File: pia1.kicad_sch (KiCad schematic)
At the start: 33 parts, among them IC20 MC14529B, IC24 74LS244N, IC25 LM393P, IC26 MC6821

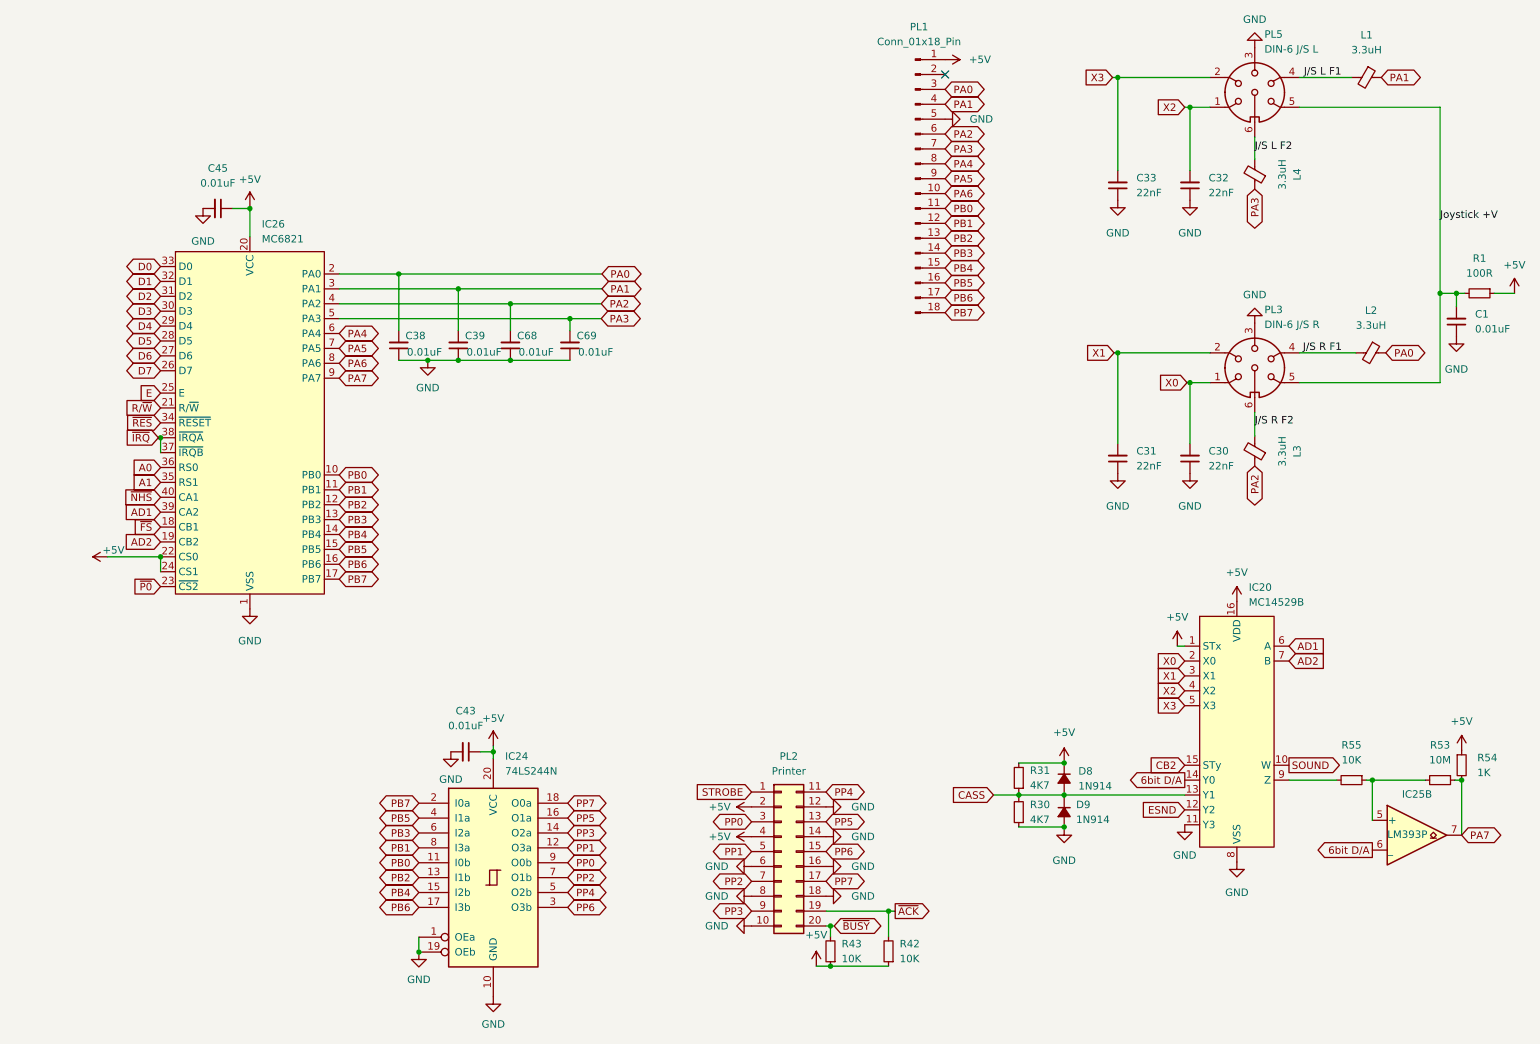
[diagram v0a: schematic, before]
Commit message: add uart to board
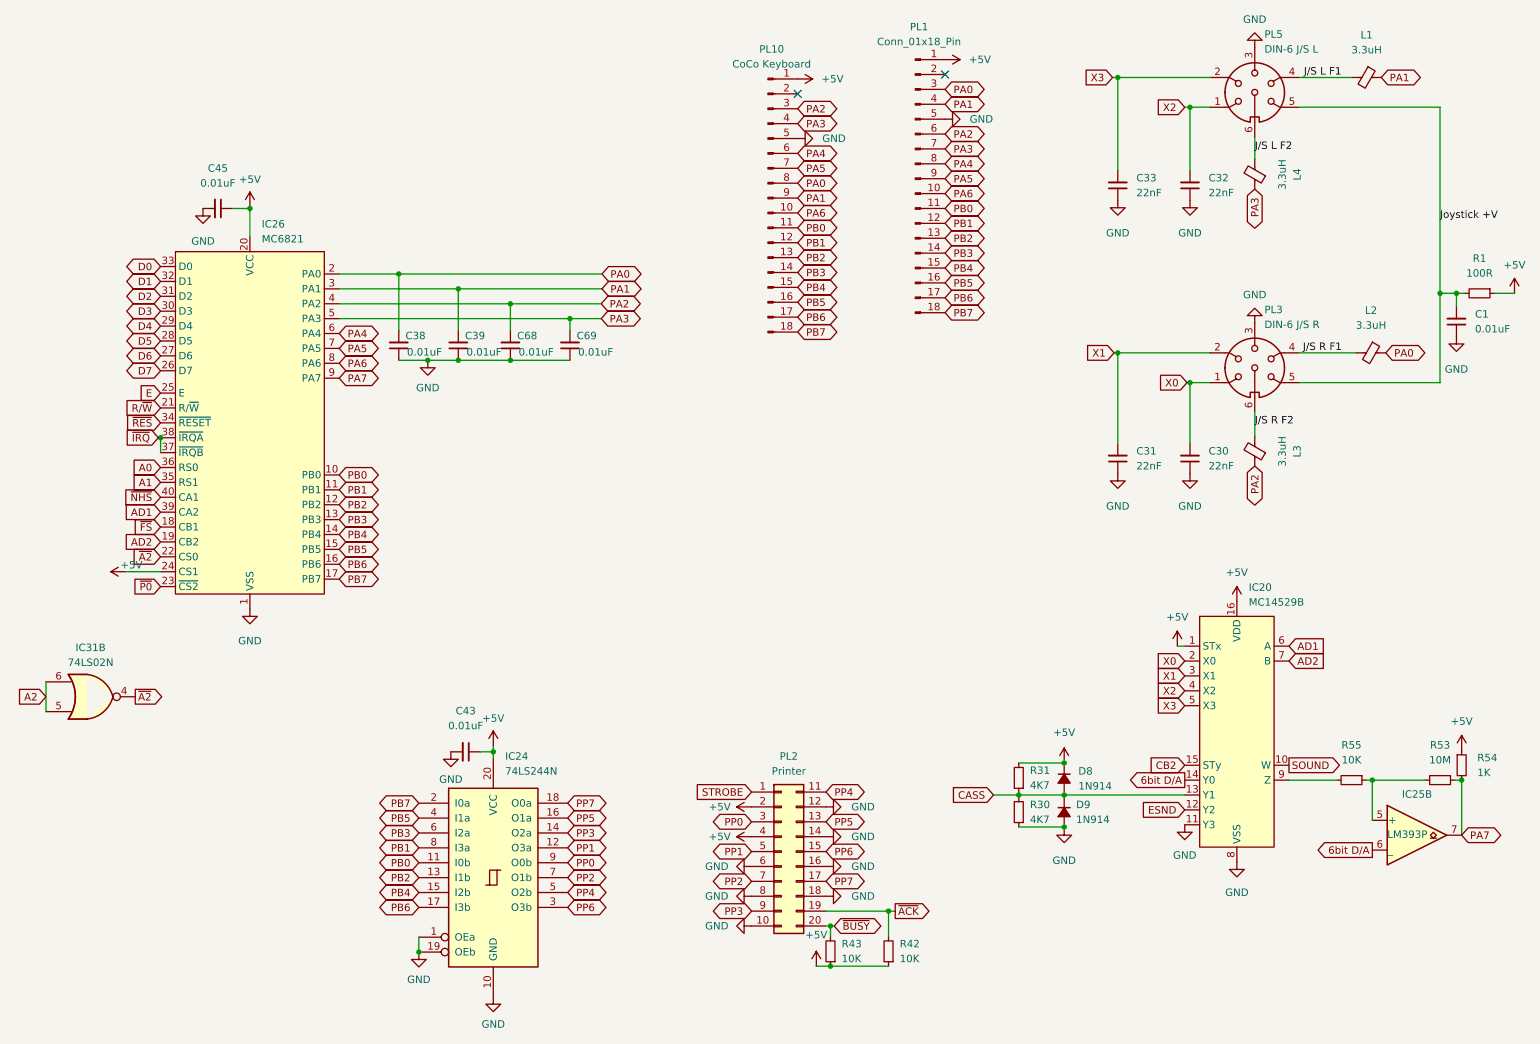
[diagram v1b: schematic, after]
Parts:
- added IC31: 74LS02N, Package_DIP:DIP-14_W7.62mm, symbol 74xx:74LS02
- added PL10: CoCo Keyboard, Connector_PinHeader_2.54mm:PinHeader_1x18_P2.54mm_Vertical, symbol Connector:Conn_01x18_Pin
- C30, C31, C32, C33: footprint Capacitor_THT:C_Disc_D5.0mm_W2.5mm_P5.00mm -> PCM_Capacitor_SMD_AKL:C_0805_2012Metric_Pad1.18x1.45mm_HandSolder; DigiKey BC2677CT-ND -> (none)
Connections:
- net +5V: now also PL10.1 (Pin_1); no longer IC26.22 (CS0)
- net GND: now also PL10.5 (Pin_5)
- net PA0: now also PL10.8 (Pin_8)
- net PA1: now also PL10.9 (Pin_9)
- net PA2: now also PL10.3 (Pin_3)
- net PA3: now also PL10.4 (Pin_4)
- net PA4: now also PL10.6 (Pin_6)
- net PA5: now also PL10.7 (Pin_7)
- net PA6: now also PL10.10 (Pin_10)
- net PB0: now also PL10.11 (Pin_11)
- net PB1: now also PL10.12 (Pin_12)
- net PB2: now also PL10.13 (Pin_13)
- net PB3: now also PL10.14 (Pin_14)
- net PB4: now also PL10.15 (Pin_15)
- net PB5: now also PL10.16 (Pin_16)
- net PB6: now also PL10.17 (Pin_17)
- net PB7: now also PL10.18 (Pin_18)
- new net A2: IC31.5, IC31.6
- new net ~{A2}: IC26.22 (CS0), IC31.4
- no-connect marks 1 -> 2

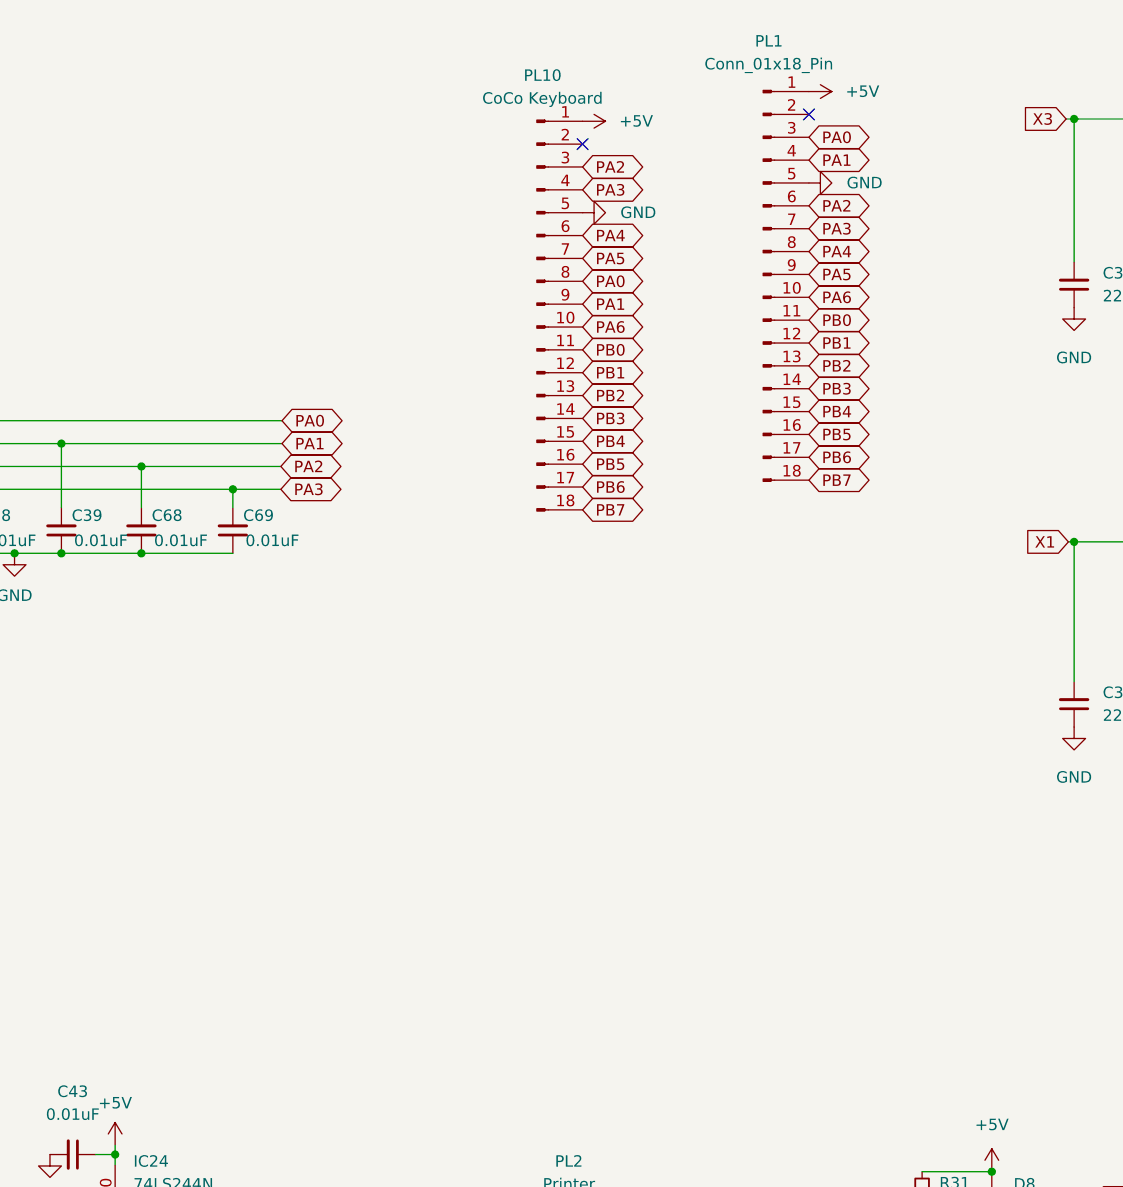
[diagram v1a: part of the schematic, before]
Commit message: rework keyboard type selection
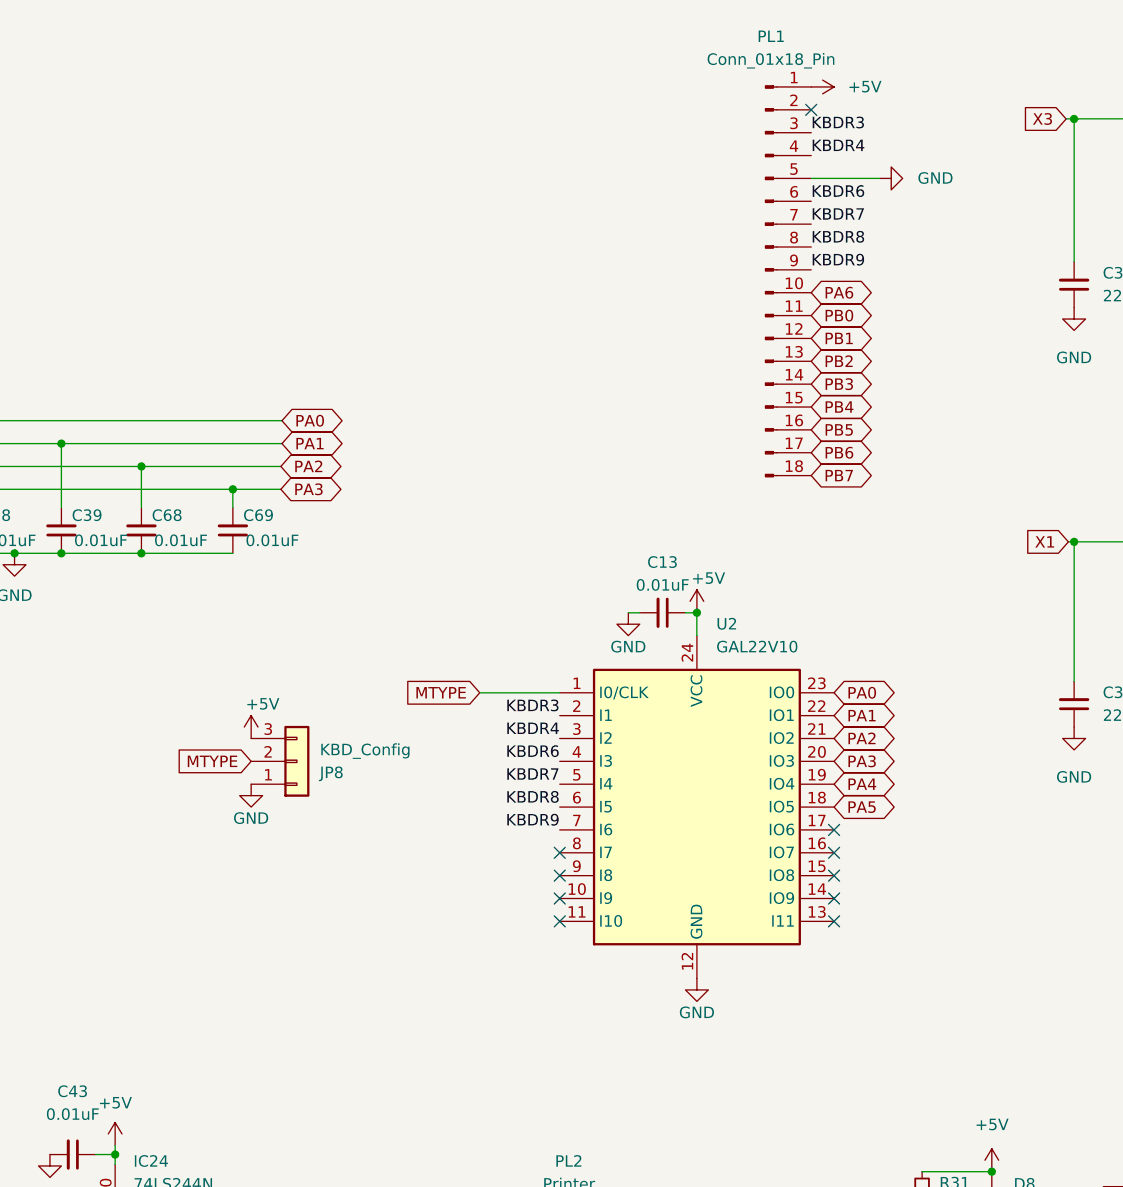
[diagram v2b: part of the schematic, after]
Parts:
- removed PL10: CoCo Keyboard, Connector_PinHeader_2.54mm:PinHeader_1x18_P2.54mm_Vertical, symbol Connector:Conn_01x18_Pin
- added C13: 0.01uF, Capacitor_THT:C_Disc_D4.3mm_W1.9mm_P5.00mm, symbol Device:C_Small
- added JP8: KBD_Config, Connector_PinHeader_2.54mm:PinHeader_1x03_P2.54mm_Vertical, symbol Connector_Generic:Conn_01x03
- added U2: GAL22V10, Package_DIP:DIP-24_W7.62mm, symbol vdg:GAL22V10
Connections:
- net +5V: now also C13.1, JP8.3 (Pin_3), U2.24 (VCC)
- net GND: now also C13.2, JP8.1 (Pin_1), U2.12 (GND)
- net PA0: now also U2.23 (IO0); no longer PL1.3 (Pin_3)
- net PA1: now also U2.22 (IO1); no longer PL1.4 (Pin_4)
- net PA2: now also U2.21 (IO2); no longer PL1.6 (Pin_6)
- net PA3: now also U2.20 (IO3); no longer PL1.7 (Pin_7)
- net PA4: now also U2.19 (IO4); no longer PL1.8 (Pin_8)
- net PA5: now also U2.18 (IO5); no longer PL1.9 (Pin_9)
- new net KBDR3: PL1.3 (Pin_3), U2.2 (I1)
- new net KBDR4: PL1.4 (Pin_4), U2.3 (I2)
- new net KBDR6: PL1.6 (Pin_6), U2.4 (I3)
- new net KBDR7: PL1.7 (Pin_7), U2.5 (I4)
- new net KBDR8: PL1.8 (Pin_8), U2.6 (I5)
- new net KBDR9: PL1.9 (Pin_9), U2.7 (I6)
- new net MTYPE: JP8.2 (Pin_2), U2.1 (I0/CLK)
- no-connect marks 2 -> 10
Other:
- moved on the sheet: PL1

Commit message: tidy up
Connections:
- net GND: now also U2.13 (I11), U2.14 (IO9), U2.15 (IO8), U2.16 (IO7), U2.17 (IO6)
- no-connect marks 10 -> 5
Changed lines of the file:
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@@
 	)
 	(junction
+		(at 181.61 111.76)
+		(diameter 0)
+		(color 0 0 0 0)
+	)
+	(junction
 		(at 265.684 145.034)
 		(diameter 0)
@@
 	)
 	(junction
+		(at 181.61 114.3)
+		(diameter 0)
+		(color 0 0 0 0)
+	)
+	(junction
 		(at 264.795 61.976)
 		(diameter 0)
@@
 	)
 	(junction
+		(at 181.61 106.68)
+		(diameter 0)
+		(color 0 0 0 0)
+	)
+	(junction
 		(at 197.866 147.574)
 		(diameter 0)
@@
 	)
 	(junction
+		(at 181.61 109.22)
+		(diameter 0)
+		(color 0 0 0 0)
+	)
+	(junction
 		(at 165.1 80.01)
 		(diameter 0)
@@
 	)
 	(no_connect
-		(at 180.34 111.76)
-	)
-	(no_connect
-		(at 180.34 109.22)
-	)
-	(no_connect
 		(at 177.8 24.13)
 	)
 	(no_connect
-		(at 180.34 114.3)
-	)
-	(no_connect
 		(at 149.86 114.3)
 	)
 	(no_connect
-		(at 180.34 106.68)
-	)
-	(no_connect
 		(at 149.86 111.76)
 	)
@@
 		(at 149.86 109.22)
 	)
-	(no_connect
-		(at 180.34 104.14)
-	)
 	(wire
 		(pts
@@
 	(wire
 		(pts
+			(xy 180.34 104.14) (xy 181.61 104.14)
+		)
+		(stroke
+			(width 0)
+			(type default)
+		)
+	)
+	(wire
+		(pts
 			(xy 74.168 61.214) (xy 94.488 61.214)
 		)
@@
 	(wire
 		(pts
+			(xy 181.61 111.76) (xy 181.61 114.3)
+		)
+		(stroke
+			(width 0)
+			(type default)
+		)
+	)
+	(wire
+		(pts
 			(xy 197.866 147.955) (xy 197.866 147.574)
 		)
@@
 	(wire
 		(pts
+			(xy 181.61 109.22) (xy 181.61 111.76)
+		)
+		(stroke
+			(width 0)
+			(type default)
+		)
+	)
+	(wire
+		(pts
 			(xy 113.538 66.294) (xy 113.538 68.326)
 		)
@@
 	(wire
 		(pts
+			(xy 180.34 106.68) (xy 181.61 106.68)
+		)
+		(stroke
+			(width 0)
+			(type default)
+		)
+	)
+	(wire
+		(pts
 			(xy 207.01 25.146) (xy 222.758 25.146)
 		)
@@
 	(wire
 		(pts
+			(xy 181.61 106.68) (xy 181.61 109.22)
+		)
+		(stroke
+			(width 0)
+			(type default)
+		)
+	)
+	(wire
+		(pts
 			(xy 274.701 61.976) (xy 271.272 61.976)
 		)
@@
 	(wire
 		(pts
+			(xy 180.34 109.22) (xy 181.61 109.22)
+		)
+		(stroke
+			(width 0)
+			(type default)
+		)
+	)
+	(wire
+		(pts
 			(xy 167.894 167.386) (xy 157.226 167.386)
 		)
@@
 	(wire
 		(pts
+			(xy 181.61 114.3) (xy 181.61 116.84)
+		)
+		(stroke
+			(width 0)
+			(type default)
+		)
+	)
+	(wire
+		(pts
 			(xy 118.872 63.754) (xy 103.378 63.754)
 		)
@@
 	(wire
 		(pts
+			(xy 180.34 114.3) (xy 181.61 114.3)
+		)
+		(stroke
+			(width 0)
+			(type default)
+		)
+	)
+	(wire
+		(pts
+			(xy 181.61 104.14) (xy 181.61 106.68)
+		)
+		(stroke
+			(width 0)
+			(type default)
+		)
+	)
+	(wire
+		(pts
 			(xy 103.378 63.754) (xy 74.168 63.754)
 		)
@@
 	(wire
 		(pts
+			(xy 180.34 111.76) (xy 181.61 111.76)
+		)
+		(stroke
+			(width 0)
+			(type default)
+		)
+	)
+	(wire
+		(pts
 			(xy 250.444 145.034) (xy 250.444 151.892)
 		)
@@
 					(unit 1)
 				)
+			)
+		)
+	)
+	(symbol
+		(lib_id "power:GND")
+		(at 181.61 116.84 0)
+		(unit 1)
+		(exclude_from_sim no)
+		(in_bom yes)
+		(on_board yes)
+		(dnp no)
+		(property "Reference" "#PWR073"
+			(at 181.61 123.19 0)
+			(effects
+				(font
+					(size 1.27 1.27)
+				)
+				(hide yes)
+			)
+		)
+		(property "Value" "GND"
+			(at 181.61 120.65 0)
+			(effects
+				(font
+					(size 1.27 1.27)
+				)
+			)
+		)
+		(property "Footprint" ""
+			(at 181.61 116.84 0)
+			(effects
+				(font
+					(size 1.27 1.27)
+				)
+				(hide yes)
+			)
+		)
+		(property "Datasheet" ""
+			(at 181.61 116.84 0)
+			(effects
+				(font
+					(size 1.27 1.27)
+				)
+				(hide yes)
+			)
+		)
+		(property "Description" ""
+			(at 181.61 116.84 0)
+			(effects
+				(font
+					(size 1.27 1.27)
+				)
+				(hide yes)
+			)
+		)
+		(pin "1"
+		)
+		(instances
+			(project "Dragon32"
+				(path "/0c3dceba-7c95-4b3d-b590-0eb581444beb/64d8d7b7-14ab-4042-9ee8-f1aec24a139c"
+					(reference "#PWR073")
+					(unit 1)
+				)

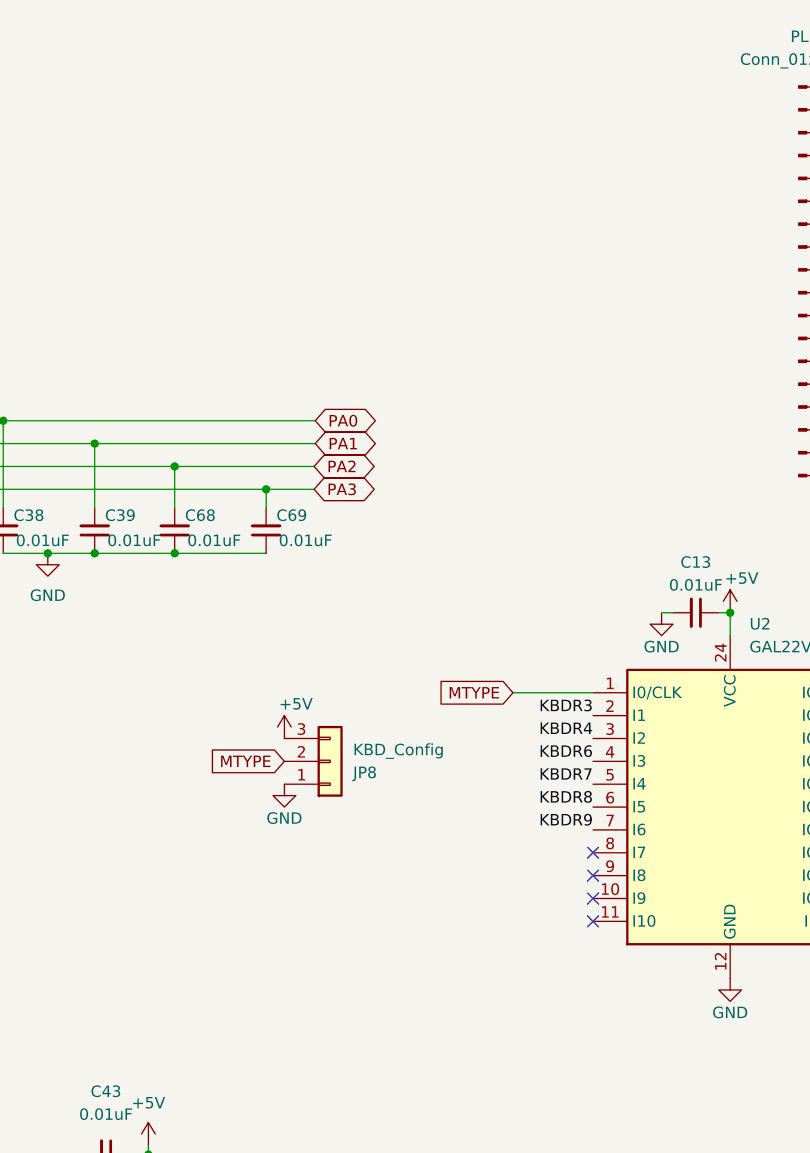
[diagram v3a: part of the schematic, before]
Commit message: pull up keyboard connections
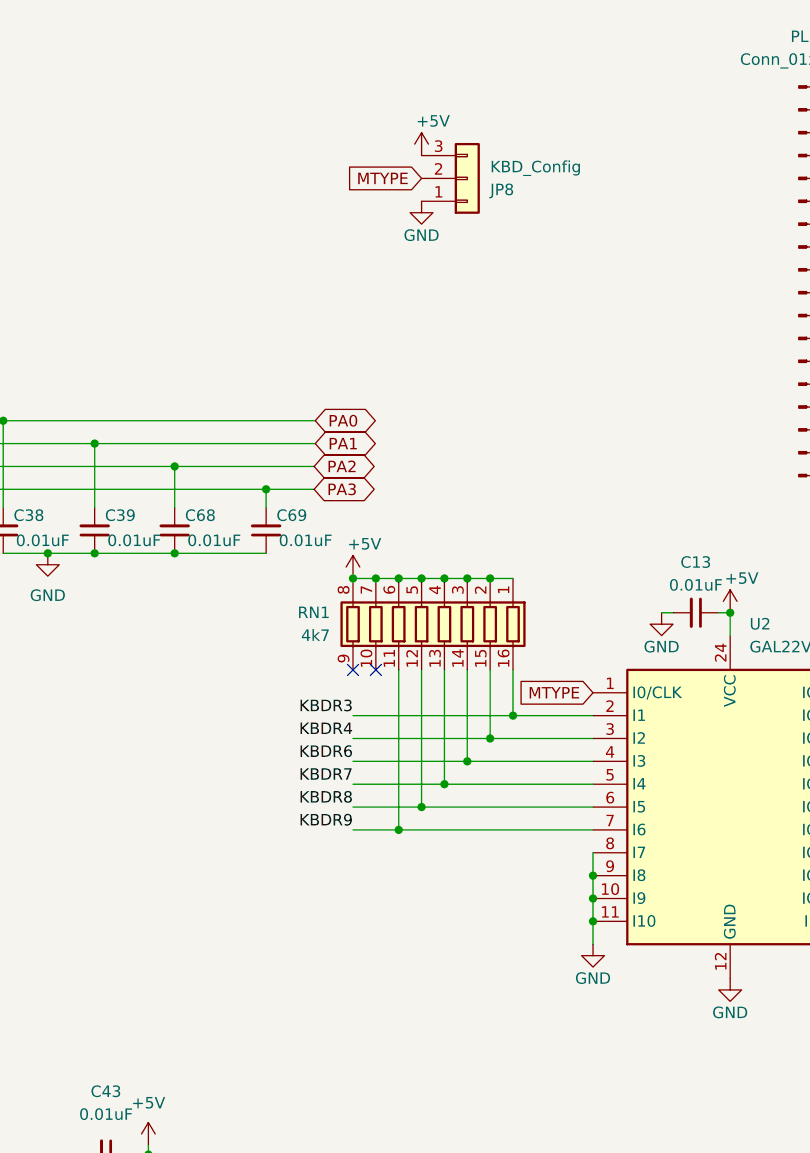
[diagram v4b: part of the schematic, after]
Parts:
- added RN1: 4k7, PCM_Resistor_SMD_AKL:R_Array_Convex_8x0602, symbol PCM_Resistor_AKL:R_8x0602_Convex
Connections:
- net +5V: now also RN1.1 (R1.1), RN1.2 (R2.1), RN1.3 (R3.1), RN1.4 (R4.1), RN1.5 (R5.1), RN1.6 (R6.1), RN1.7 (R7.1), RN1.8 (R8.1)
- net GND: now also U2.10 (I9), U2.11 (I10), U2.8 (I7), U2.9 (I8)
- net KBDR3: now also RN1.16 (R1.2)
- net KBDR4: now also RN1.15 (R2.2)
- net KBDR6: now also RN1.14 (R3.2)
- net KBDR7: now also RN1.13 (R4.2)
- net KBDR8: now also RN1.12 (R5.2)
- net KBDR9: now also RN1.11 (R6.2)
- no-connect marks 5 -> 3
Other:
- moved on the sheet: JP8
